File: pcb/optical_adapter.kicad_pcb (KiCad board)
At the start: 4 copper layers, 50 x 20 mm, 24 parts, among them J1 Conn_01x06_Pin, Q1 BC847, Q2 BC847, Q3 BC857, Q5 IRLML2060, U1 LM1117MP-3.3

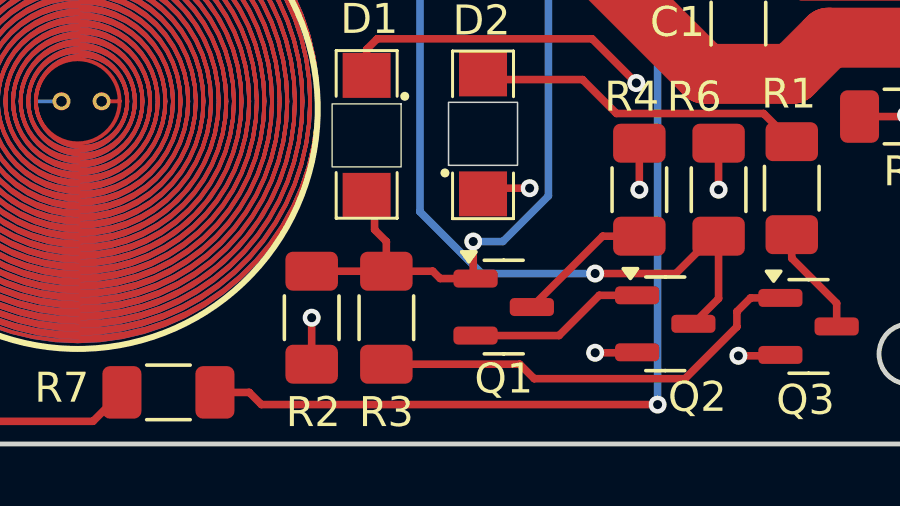
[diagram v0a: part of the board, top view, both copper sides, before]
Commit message: Add solder bridge between TX and RX circuit
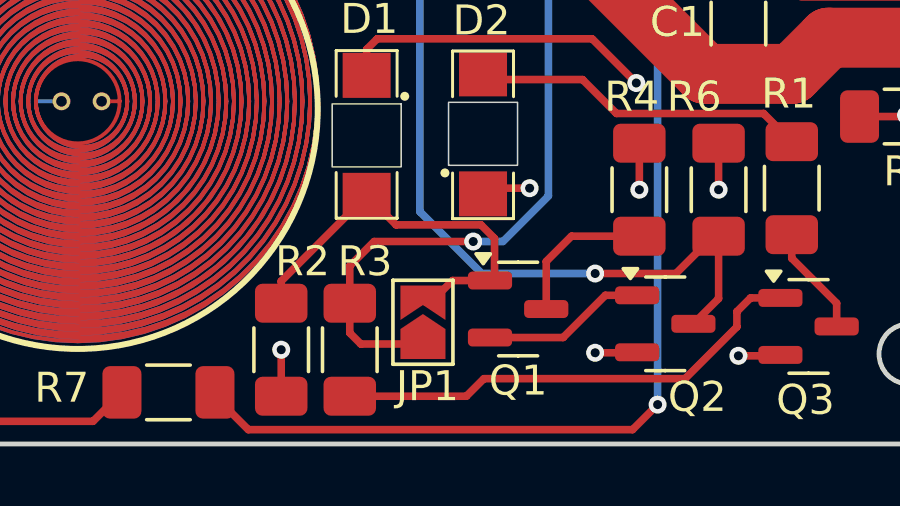
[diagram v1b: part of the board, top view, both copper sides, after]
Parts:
- added JP1: SolderJumper_2_Bridged, Jumper:SolderJumper-2_P1.3mm_Open_TrianglePad1.0x1.5mm, F.Cu at (129.3, 103.5)
- moved R3 1.62 mm to (126.9, 104.4)
- moved R2 1.47 mm to (124.6, 104.4)
- moved Q1 0.48 mm to (132.5, 103.1)
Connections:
- D1 pad 2: /TX -> Net-(D1-A)
- Q1 pad 1: /TX -> Net-(D1-A)
- R2 pad 1: /TX -> Net-(D1-A)
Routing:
- net Net-(D1-A): track 0.00 -> 13.7 mm
- net Net-(Q3-B): track 14.7 -> 16.0 mm
- net /WAKE: track 31.6 -> 32.3 mm

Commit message: Fix the coil active LED
Changed to 150 Ohm to better suite the amber LED and fix incorrect
rotation.
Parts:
- R8: value 91 -> 150
- turned D3 to 90 degrees
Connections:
- D3 pad 1: +5V -> Net-(D3-K)
- D3 pad 2: Net-(D3-A) -> +5V
- R8 pad 1: Net-(D3-A) -> Net-(D3-K)
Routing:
- net Net-(D3-K): track 0.00 -> 2.79 mm
- net Net-(D3-A): track 2.56 -> 0.00 mm
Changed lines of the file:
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@@
 	)
 	(net 0 "")
-	(net 1 "Net-(D3-A)")
+	(net 1 "Net-(D3-K)")
 	(net 2 "Net-(D4-A)")
 	(net 3 "/WAKE")
@@
 			)
 		)
-		(property "Value" "91"
+		(property "Value" "150"
 			(at 0 1.82 90)
 			(layer "F.Fab")
@@
 			)
 		)
-		(property "MFRNO" "CRCW120691R0JNEA"
+		(property "MFRNO" "CRCW1206150RJNEA"
 			(at 0 0 270)
 			(unlocked yes)
@@
 			)
 		)
-		(property "MOUSERNO" "71-CRCW1206J-91-E3"
+		(property "MOUSERNO" "71-CRCW1206J-150-E3"
 			(at 0 0 270)
 			(unlocked yes)
@@
 			(layers "F.Cu" "F.Mask" "F.Paste")
 			(roundrect_rratio 0.192308)
-			(net 1 "Net-(D3-A)")
+			(net 1 "Net-(D3-K)")
 			(pintype "passive")
 		)
@@
 			)
 		)
-		(property "MOUSERNO" "71-CRCW1206J-220-E3 "
+		(property "MOUSERNO" "71-CRCW1206J-220-E3"
 			(at 0 0 180)
 			(unlocked yes)
@@
 	(footprint "LED_SMD:LED_1206_3216Metric_Pad1.42x1.75mm_HandSolder"
 		(layer "F.Cu")
-		(at 107.1372 91.694 -90)
+		(at 107.1372 91.694 90)
 		(descr "LED SMD 1206 (3216 Metric), square (rectangular) end terminal, IPC-7351 nominal, (Body size source: http://www.tortai-tech.com/upload/download/2011102023233369053.pdf), generated with kicad-footprint-generator")
 		(tags "LED handsolder")
 		(property "Reference" "D3"
-			(at 1.9812 -2.032 180)
+			(at -1.9304 2.0828 180)
 			(layer "F.SilkS")
 			(effects
@@
 		)
 		(property "Datasheet" "https://www.we-online.com/components/products/datasheet/150120AS75000.pdf"
-			(at 0 0 270)
+			(at 0 0 90)
 			(unlocked yes)
 			(layer "F.Fab")
@@
 		)
 		(property "Description" "Light emitting diode"
-			(at 0 0 270)
+			(at 0 0 90)
 			(unlocked yes)
 			(layer "F.Fab")
@@
 		)
 		(property "LCSC" ""
-			(at 0 0 270)
+			(at 0 0 90)
 			(unlocked yes)
 			(layer "F.Fab")
@@
 		)
 		(property "MFRNO" "150120AS75000"
-			(at 0 0 270)
+			(at 0 0 90)
 			(unlocked yes)
 			(layer "F.Fab")
@@
 		)
 		(property "MOUSERNO" "710-150120AS75000 "
-			(at 0 0 270)
+			(at 0 0 90)
 			(unlocked yes)
 			(layer "F.Fab")
@@
 		(attr smd)
 		(fp_line
-			(start -2.46 1.135)
-			(end 1.6 1.135)
+			(start 1.6 -1.135)
+			(end -2.46 -1.135)
 			(stroke
 				(width 0.12)
@@
 		)
 		(fp_line
-			(start 1.6 -1.135)
-			(end -2.46 -1.135)
+			(start -2.46 1.135)
+			(end 1.6 1.135)
 			(stroke
 				(width 0.12)
@@
 		)
 		(fp_line
-			(start -2.45 1.13)
-			(end -2.45 -1.13)
+			(start 2.45 -1.13)
+			(end 2.45 1.13)
 			(stroke
 				(width 0.05)
@@
 		)
 		(fp_line
-			(start 2.45 1.13)
-			(end -2.45 1.13)
+			(start -2.45 -1.13)
+			(end 2.45 -1.13)
 			(stroke
 				(width 0.05)
@@
 		)
 		(fp_line
-			(start -2.45 -1.13)
-			(end 2.45 -1.13)
+			(start 2.45 1.13)
+			(end -2.45 1.13)
 			(stroke
 				(width 0.05)
@@
 		)
 		(fp_line
-			(start 2.45 -1.13)
-			(end 2.45 1.13)
+			(start -2.45 1.13)
+			(end -2.45 -1.13)
 			(stroke
 				(width 0.05)
@@
 		)
 		(fp_line
-			(start -1.6 0.8)
-			(end 1.6 0.8)
+			(start 1.6 -0.8)
+			(end -1.2 -0.8)
 			(stroke
 				(width 0.1)
@@
 		)
 		(fp_line
-			(start 1.6 0.8)
-			(end 1.6 -0.8)
+			(start -1.2 -0.8)
+			(end -1.6 -0.4)
 			(stroke
 				(width 0.1)
@@
 		)
 		(fp_line
-			(start -1.2 -0.8)
-			(end -1.6 -0.4)
+			(start 1.6 0.8)
+			(end 1.6 -0.8)
 			(stroke
 				(width 0.1)
@@
 		)
 		(fp_line
-			(start 1.6 -0.8)
-			(end -1.2 -0.8)
+			(start -1.6 0.8)
+			(end 1.6 0.8)
 			(stroke
 				(width 0.1)
@@
 		)
 		(pad "1" smd roundrect
-			(at -1.4875 0 270)
+			(at -1.4875 0 90)
 			(size 1.425 1.75)
 			(layers "F.Cu" "F.Mask" "F.Paste")
 			(roundrect_rratio 0.175439)
-			(net 8 "+5V")
+			(net 1 "Net-(D3-K)")
 			(pinfunction "K")
 			(pintype "passive")
 		)
 		(pad "2" smd roundrect
-			(at 1.4875 0 270)
+			(at 1.4875 0 90)
 			(size 1.425 1.75)
 			(layers "F.Cu" "F.Mask" "F.Paste")
 			(roundrect_rratio 0.175439)
-			(net 1 "Net-(D3-A)")
+			(net 8 "+5V")
 			(pinfunction "A")
 			(pintype "passive")
@@
 	)
 	(segment
-		(start 106.1212 94.0308)
-		(end 106.9705 93.1815)
+		(start 107.1372 94.488)
+		(end 107.1372 93.1815)
 		(width 0.254)
 		(layer "F.Cu")
@@
 	)
 	(segment
+		(start 106.4012 95.224)
+		(end 107.1372 94.488)
+		(width 0.254)
+		(layer "F.Cu")
+		(net 1)
+	)
+	(segment
 		(start 106.1212 95.224)
-		(end 106.1212 94.0308)
+		(end 106.4012 95.224)
 		(width 0.254)
 		(layer "F.Cu")
@@
 	)
 	(segment
+		(start 107.1372 90.2065)
+		(end 107.1372 91.6432)
+		(width 0.254)
+		(layer "F.Cu")
+		(net 8)
+	)
+	(segment
 		(start 134.7216 89.662)
 		(end 134.7216 91.2368)
@@
 		(layer "F.Cu")
 		(net 8)
-	)
-	(segment
-		(start 107.1372 91.6432)
-		(end 107.1372 90.2065)
-		(width 0.548)
-		(layer "F.Cu")
-		(net 8)

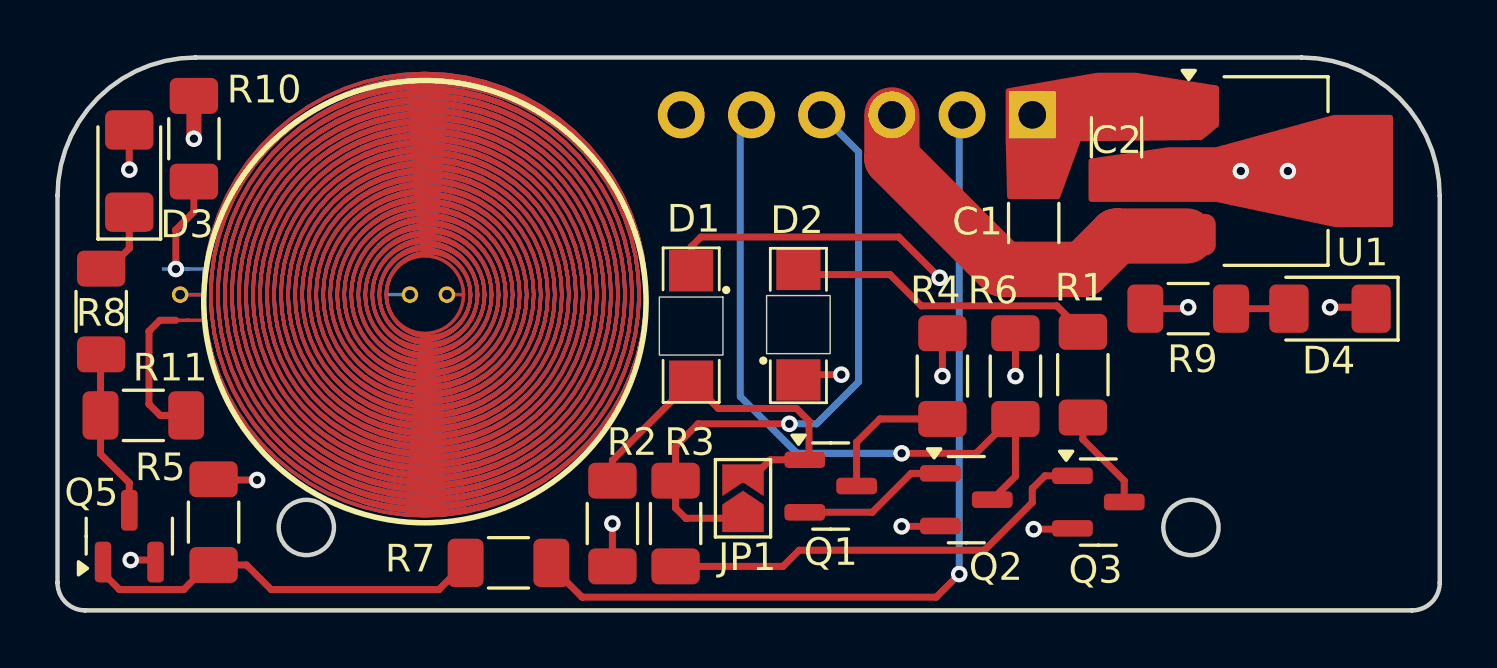
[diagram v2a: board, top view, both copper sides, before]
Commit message: Update symbols
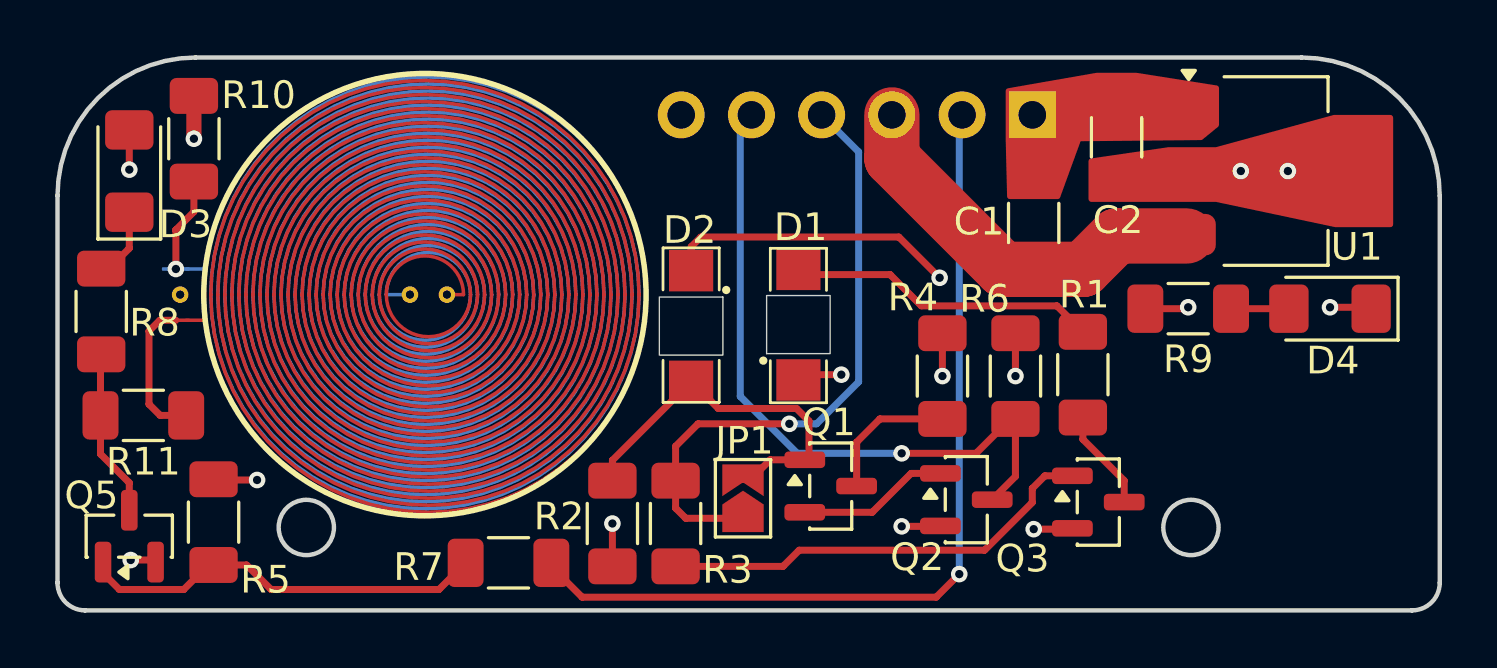
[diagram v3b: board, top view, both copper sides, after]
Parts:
- L1: footprint footprints:26_turn_16_dia_5_mil -> PCB Coils:4l_26_turn_16_dia_5_mil

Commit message: Move the coil wake up signal to RTS
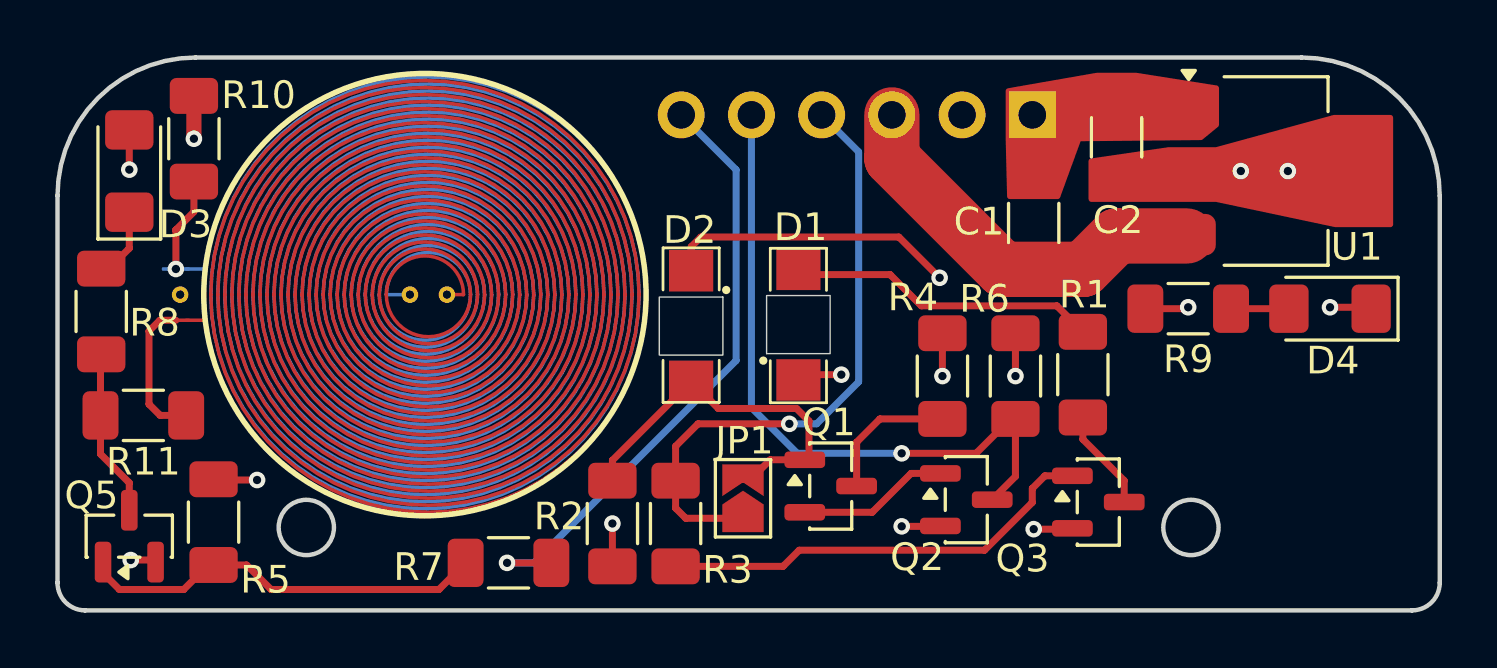
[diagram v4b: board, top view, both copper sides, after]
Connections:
- J1 pad 2: /WAKE -> unconnected-(J1-Pin_2-Pad2)
- J1 pad 6: unconnected-(J1-Pin_6-Pad6) -> /WAKE
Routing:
- net /WAKE: track 32.3 -> 22.8 mm
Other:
- board text added: "EN RX TX 5V NC GND"
- board text removed: "NC RX TX 5V WAKE GND"
